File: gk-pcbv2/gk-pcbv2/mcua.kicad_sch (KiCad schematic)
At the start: 21 parts, among them SW1 SW_Push, SW2 SW_Push, U4 STM32H747BITx, Y1 16MHz, Y2 32.768kHz R26-32.768-12.5

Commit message: more v2 pcb changes
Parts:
- removed SW2: SW_Push, gk:Tactile Switch 6x3.5mm, symbol Switch:SW_Push
- Y2: footprint Crystal:Crystal_C26-LF_D2.1mm_L6.5mm_Horizontal_1EP_style2 -> Crystal:Crystal_C26-LF_D2.1mm_L6.5mm_Horizontal_1EP_style1
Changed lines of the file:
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@@
   (junction (at 48.26 172.72) (diameter 0) (color 0 0 0 0)
-  )
-  (junction (at 25.4 186.69) (diameter 0) (color 0 0 0 0)
   )
   (junction (at 20.32 123.19) (diameter 0) (color 0 0 0 0)
@@
     (stroke (width 0) (type default))
   )
-  (wire (pts (xy 21.59 181.61) (xy 21.59 176.53))
-    (stroke (width 0) (type default))
-  )
   (wire (pts (xy 20.32 34.29) (xy 20.32 43.18))
     (stroke (width 0) (type default))
@@
     (stroke (width 0) (type default))
   )
-  (wire (pts (xy 16.51 179.07) (xy 16.51 181.61))
-    (stroke (width 0) (type default))
-  )
   (wire (pts (xy 116.84 160.02) (xy 124.46 160.02))
     (stroke (width 0) (type default))
@@
     (stroke (width 0) (type default))
   )
-  (wire (pts (xy 21.59 176.53) (xy 25.4 176.53))
-    (stroke (width 0) (type default))
-  )
   (wire (pts (xy 48.26 160.02) (xy 48.26 165.1))
     (stroke (width 0) (type default))
@@
   )
   (wire (pts (xy 48.26 172.72) (xy 60.96 172.72))
-    (stroke (width 0) (type default))
-  )
-  (wire (pts (xy 16.51 181.61) (xy 21.59 181.61))
     (stroke (width 0) (type default))
   )
@@
       (effects (font (size 1.27 1.27)))
     )
-    (property "Footprint" "Crystal:Crystal_C26-LF_D2.1mm_L6.5mm_Horizontal_1EP_style2" (at 160.02 21.59 0)
+    (property "Footprint" "Crystal:Crystal_C26-LF_D2.1mm_L6.5mm_Horizontal_1EP_style1" (at 160.02 21.59 0)
       (effects (font (size 1.27 1.27)) hide)
     )
@@
         (path "/08730ac6-6084-459f-bdf1-86b322355ede/d577d9fa-dd9e-43ac-82a3-80fa54936848"
           (reference "Y2") (unit 1)
-        )
-      )
-    )
-  )
-  (symbol (lib_id "power:VCC") (at 16.51 179.07 0) (unit 1)
-    (in_bom yes) (on_board yes) (dnp no) (fields_autoplaced)
-    (property "Reference" "#PWR05" (at 16.51 182.88 0)
-      (effects (font (size 1.27 1.27)) hide)
-    )
-    (property "Value" "VCC" (at 16.51 175.26 0)
-      (effects (font (size 1.27 1.27)))
-    )
-    (property "Footprint" "" (at 16.51 179.07 0)
-      (effects (font (size 1.27 1.27)) hide)
-    )
-    (property "Datasheet" "" (at 16.51 179.07 0)
-      (effects (font (size 1.27 1.27)) hide)
-    )
-    (pin "1")
-    (instances
-      (project "gk-pcbv2"
-        (path "/08730ac6-6084-459f-bdf1-86b322355ede/d577d9fa-dd9e-43ac-82a3-80fa54936848"
-          (reference "#PWR05") (unit 1)
         )
       )
@@
         )
       )
-    )
-  )
-  (symbol (lib_id "Switch:SW_Push") (at 25.4 181.61 270) (unit 1)
-    (in_bom yes) (on_board yes) (dnp no) (fields_autoplaced)
-    (property "Reference" "SW2" (at 29.21 180.34 90)
-      (effects (font (size 1.27 1.27)) (justify left))
-    )
-    (property "Value" "SW_Push" (at 29.21 182.88 90)
-      (effects (font (size 1.27 1.27)) (justify left))
-    )
-    (property "Footprint" "gk:Tactile Switch 6x3.5mm" (at 30.48 181.61 0)
-      (effects (font (size 1.27 1.27)) hide)
-    )
-    (property "Datasheet" "~" (at 30.48 181.61 0)
-      (effects (font (size 1.27 1.27)) hide)
-    )
-    (pin "1")
-    (pin "2")
-    (instances
-      (project "gk-pcbv2"
-        (path "/08730ac6-6084-459f-bdf1-86b322355ede/d577d9fa-dd9e-43ac-82a3-80fa54936848"
-          (reference "SW2") (unit 1)
-        )
-      )

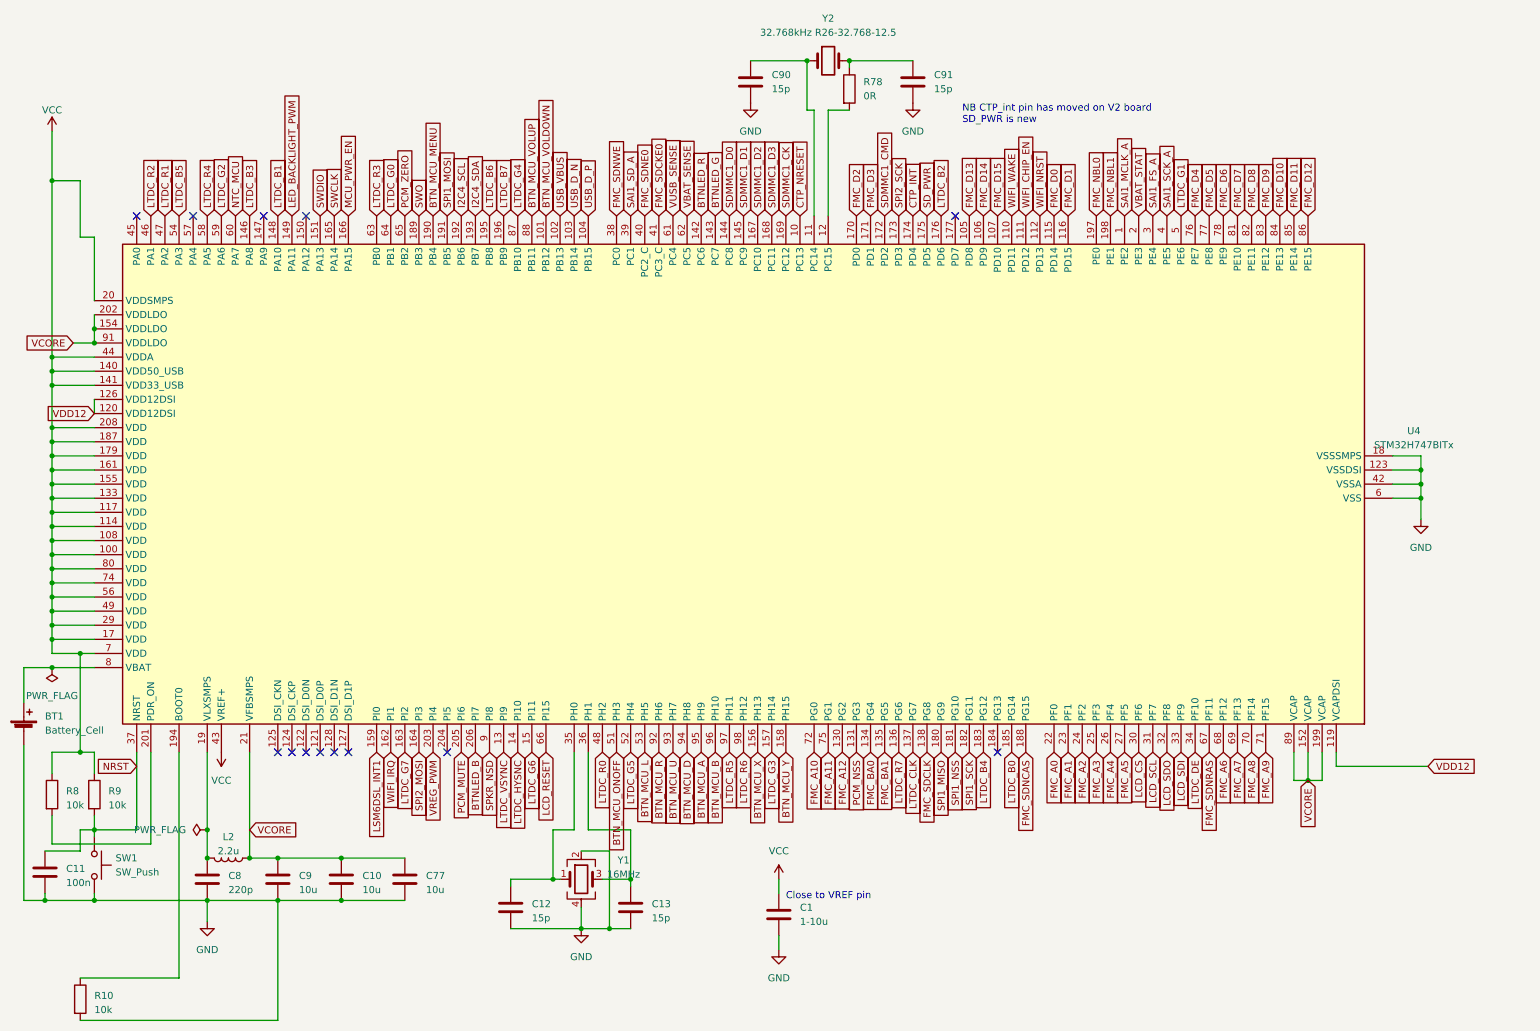
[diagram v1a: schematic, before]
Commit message: update pcb for SMPS supplies LDO configuration
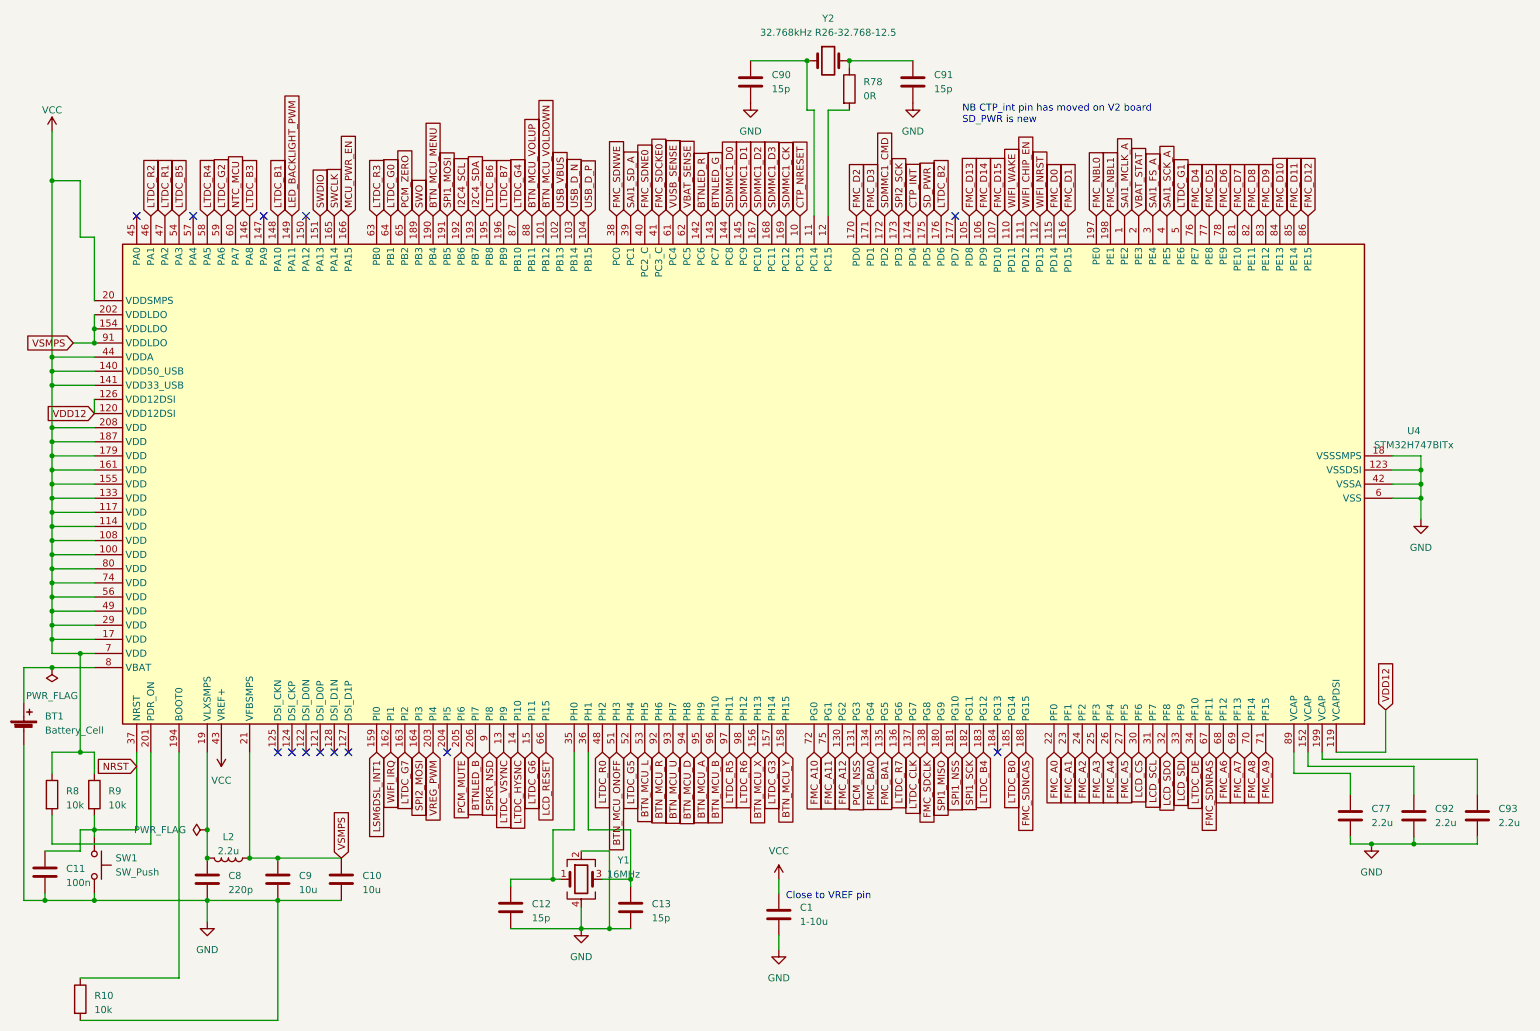
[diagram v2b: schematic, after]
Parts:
- added C92, C93: 2.2u, Capacitor_SMD:C_0603_1608Metric, symbol Device:C
- C77: value 10u -> 2.2u; footprint Capacitor_SMD:C_0805_2012Metric -> Capacitor_SMD:C_0603_1608Metric
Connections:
- net GND: now also C92.2, C93.2
- net VCORE renamed VSMPS
- net VSMPS: no longer C77.1, U4.152 (VCAP), U4.199 (VCAP), U4.89 (VCAP)
- new net: C92.1, U4.152 (VCAP)
- new net: C93.1, U4.199 (VCAP)
- new net: C77.1, U4.89 (VCAP)

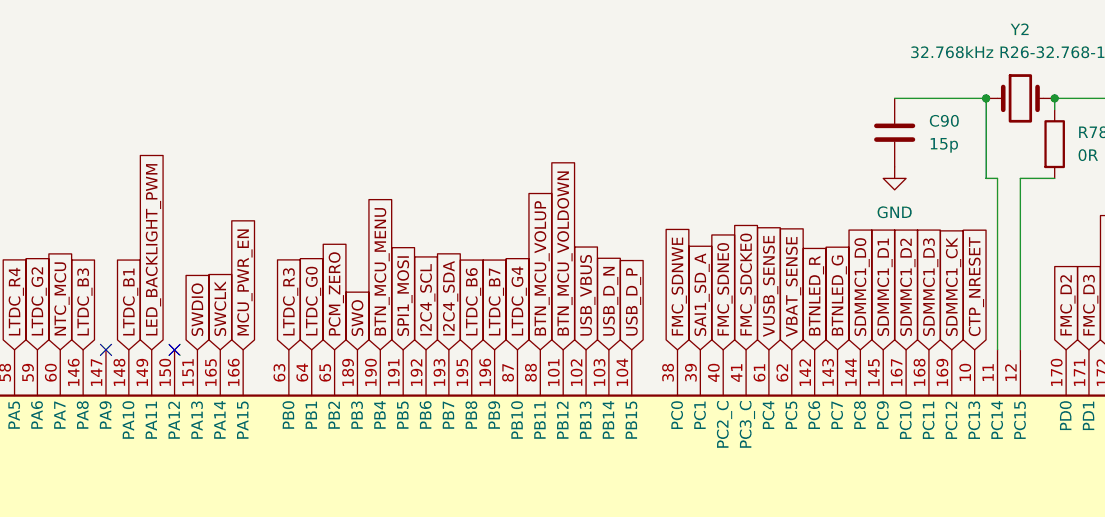
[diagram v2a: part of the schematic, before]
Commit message: change voldown button to GPIOA12
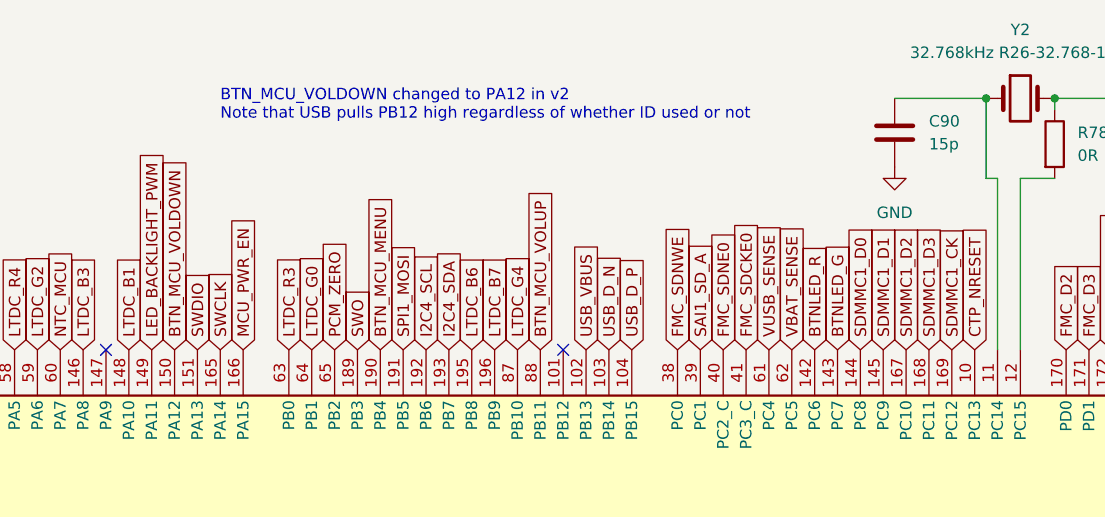
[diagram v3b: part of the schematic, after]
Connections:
- net BTN_MCU_VOLDOWN: now also U4.150 (PA12); no longer U4.101 (PB12)
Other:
- note added: "BTN_MCU_VOLDOWN changed to PA12 in v2 Note that USB pulls PB12 high regardless of whether ID used or not"
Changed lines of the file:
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@@
   (no_connect (at 68.58 146.05))
   (no_connect (at 71.12 146.05))
+  (no_connect (at 109.22 49.53))
   (no_connect (at 45.72 49.53))
   (no_connect (at 190.5 146.05))
-  (no_connect (at 66.04 49.53))
   (no_connect (at 35.56 49.53))
   (no_connect (at 63.5 146.05))
@@
     (effects (font (size 1.27 1.27)) (justify left bottom))
   )
+  (text "BTN_MCU_VOLDOWN changed to PA12 in v2\nNote that USB pulls PB12 high regardless of whether ID used or not"
+    (at 71.12 24.13 0)
+    (effects (font (size 1.27 1.27)) (justify left bottom))
+  )
   (global_label "SPI2_SCK" (shape input) (at 172.72 49.53 90) (fields_autoplaced)
     (effects (font (size 1.27 1.27)) (justify left))
@@
     )
   )
-  (global_label "BTN_MCU_VOLDOWN" (shape input) (at 109.22 49.53 90) (fields_autoplaced)
-    (effects (font (size 1.27 1.27)) (justify left))
-    (property "Intersheetrefs" "${INTERSHEET_REFS}" (at 109.22 28.2394 90)
-      (effects (font (size 1.27 1.27)) (justify left) hide)
-    )
+  (global_label "BTN_MCU_VOLDOWN" (shape input) (at 66.04 49.53 90) (fields_autoplaced)
+    (effects (font (size 1.27 1.27)) (justify left))
+    (property "Intersheetrefs" "${INTERSHEET_REFS}" (at 66.04 28.2394 90)
+      (effects (font (size 1.27 1.27)) (justify left) hide)
+    )

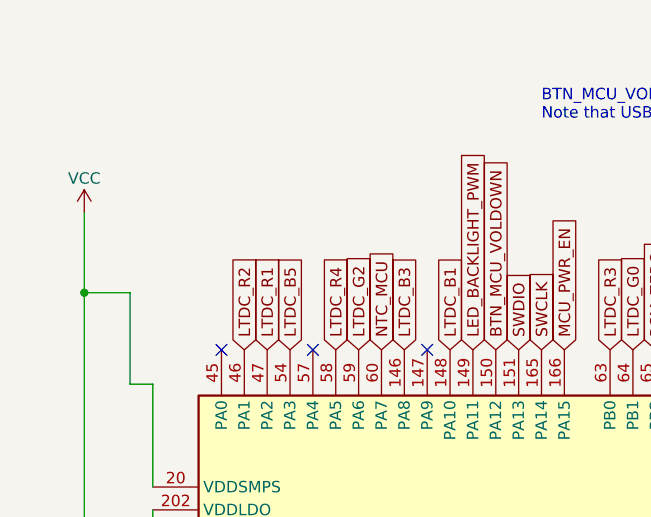
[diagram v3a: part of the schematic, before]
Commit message: add uart4tx output
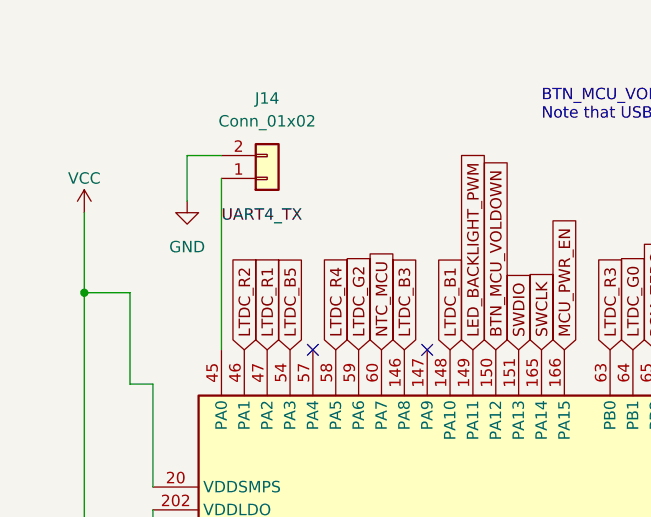
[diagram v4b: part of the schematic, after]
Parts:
- added J14: Conn_01x02, Connector_PinHeader_2.54mm:PinHeader_1x02_P2.54mm_Vertical, symbol Connector_Generic:Conn_01x02
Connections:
- net GND: now also J14.2 (Pin_2)
- net UART4_TX: now reaches U4.45 (PA0)
- net UART4_TX: now also J14.1 (Pin_1)
- no-connect marks 13 -> 12
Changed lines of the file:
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@@
   (no_connect (at 45.72 49.53))
   (no_connect (at 190.5 146.05))
-  (no_connect (at 35.56 49.53))
   (no_connect (at 63.5 146.05))
   (no_connect (at 66.04 146.05))
@@
   (no_connect (at 60.96 146.05))
   (no_connect (at 182.88 49.53))
+  (wire (pts (xy 31.75 27.94) (xy 31.75 33.02))
+    (stroke (width 0) (type default))
+  )
   (wire (pts (xy 24.13 72.39) (xy 27.94 72.39))
     (stroke (width 0) (type default))
@@
     (stroke (width 0) (type default))
   )
+  (wire (pts (xy 35.56 27.94) (xy 31.75 27.94))
+    (stroke (width 0) (type default))
+  )
   (wire (pts (xy 115.57 163.83) (xy 120.65 163.83))
     (stroke (width 0) (type default))
@@
   )
   (wire (pts (xy 157.48 49.53) (xy 157.48 30.48))
+    (stroke (width 0) (type default))
+  )
+  (wire (pts (xy 35.56 30.48) (xy 35.56 49.53))
     (stroke (width 0) (type default))
   )
@@
     (effects (font (size 1.27 1.27)) (justify left bottom))
   )
+  (label "UART4_TX" (at 35.56 35.56 0) (fields_autoplaced)
+    (effects (font (size 1.27 1.27)) (justify left bottom))
+  )
   (global_label "SPI2_SCK" (shape input) (at 172.72 49.53 90) (fields_autoplaced)
     (effects (font (size 1.27 1.27)) (justify left))
@@
     (property "Intersheetrefs" "${INTERSHEET_REFS}" (at 78.74 38.6414 90)
       (effects (font (size 1.27 1.27)) (justify left) hide)
+    )
+  )
+  (symbol (lib_id "power:GND") (at 31.75 33.02 0) (unit 1)
+    (in_bom yes) (on_board yes) (dnp no) (fields_autoplaced)
+    (property "Reference" "#PWR0102" (at 31.75 39.37 0)
+      (effects (font (size 1.27 1.27)) hide)
+    )
+    (property "Value" "GND" (at 31.75 38.1 0)
+      (effects (font (size 1.27 1.27)))
+    )
+    (property "Footprint" "" (at 31.75 33.02 0)
+      (effects (font (size 1.27 1.27)) hide)
+    )
+    (property "Datasheet" "" (at 31.75 33.02 0)
+      (effects (font (size 1.27 1.27)) hide)
+    )
+    (pin "1")
+    (instances
+      (project "gk-pcbv2"
+        (path "/08730ac6-6084-459f-bdf1-86b322355ede/d577d9fa-dd9e-43ac-82a3-80fa54936848"
+          (reference "#PWR0102") (unit 1)
+        )
+      )
     )
   )
@@
         )
       )
+    )
+  )
+  (symbol (lib_id "Connector_Generic:Conn_01x02") (at 40.64 30.48 0) (mirror x) (unit 1)
+    (in_bom yes) (on_board yes) (dnp no) (fields_autoplaced)
+    (property "Reference" "J14" (at 40.64 21.59 0)
+      (effects (font (size 1.27 1.27)))
+    )
+    (property "Value" "Conn_01x02" (at 40.64 24.13 0)
+      (effects (font (size 1.27 1.27)))
+    )
+    (property "Footprint" "Connector_PinHeader_2.54mm:PinHeader_1x02_P2.54mm_Vertical" (at 40.64 30.48 0)
+      (effects (font (size 1.27 1.27)) hide)
+    )
+    (property "Datasheet" "~" (at 40.64 30.48 0)
+      (effects (font (size 1.27 1.27)) hide)
+    )
+    (pin "1")
+    (pin "2")
+    (instances
+      (project "gk-pcbv2"
+        (path "/08730ac6-6084-459f-bdf1-86b322355ede/d577d9fa-dd9e-43ac-82a3-80fa54936848"
+          (reference "J14") (unit 1)
+        )
+      )
